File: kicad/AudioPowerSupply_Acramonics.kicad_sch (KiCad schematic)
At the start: 32 parts, among them J1 Conn_01x02_Pin, J6 GND 48V, J7 Conn_01x03_Pin, J8 Conn_01x03_Pin, T1 12-0-12V, U1 LM7815_TO220, U2 LM7915_TO220, U3 LM317_TO-220

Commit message: Put 48V circuit on separate diagram
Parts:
- removed C10, C11: 100nF, Capacitor_THT:C_Rect_L7.2mm_W3.0mm_P5.00mm_FKS2_FKP2_MKS2_MKP2, symbol Device:C_Small
- removed C3, C4: 100uF 100V, Capacitor_THT:CP_Radial_D12.5mm_P5.00mm, symbol Device:C_Polarized_Small
- removed C5: 220uF 100V, Capacitor_THT:CP_Radial_D12.5mm_P5.00mm, symbol Device:C_Polarized_Small
- removed D1: 1N4003, Diode_THT:D_DO-41_SOD81_P10.16mm_Horizontal, symbol Diode:1N4003
- removed D2, D3, D4, D5: 1N4004, Diode_THT:D_DO-41_SOD81_P10.16mm_Horizontal, symbol Diode:1N4004
- removed J6: GND 48V, Connector_Molex:Molex_KK-254_AE-6410-02A_1x02_P2.54mm_Vertical, symbol Connector:Conn_01x02_Pin
- removed R1: 8K2 2W, Resistor_THT:R_Axial_DIN0414_L11.9mm_D4.5mm_P15.24mm_Horizontal, symbol Device:R_Small
- removed R2: 240R, Resistor_THT:R_Axial_DIN0207_L6.3mm_D2.5mm_P10.16mm_Horizontal, symbol Device:R_Small
- removed U3: LM317_TO-220, Package_TO_SOT_THT:TO-220-3_Vertical, symbol Regulator_Linear:LM317_TO-220
- J1: footprint (none) -> TerminalBlock_Altech:Altech_AK100_1x02_P5.00mm
- J7, J8: footprint TerminalBlock_4Ucon:TerminalBlock_4Ucon_1x03_P3.50mm_Horizontal -> TerminalBlock_Altech:Altech_AK100_1x03_P5.00mm
- renumbered C6 to C3, C7 to C4, C12 to C5, C13 to C6, C8 to C7, C9 to C8, D6 to D1, D7 to D2, D8 to D3, D9 to D4
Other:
- added sheet 48V-Booster (48V-Booster.kicad_sch)

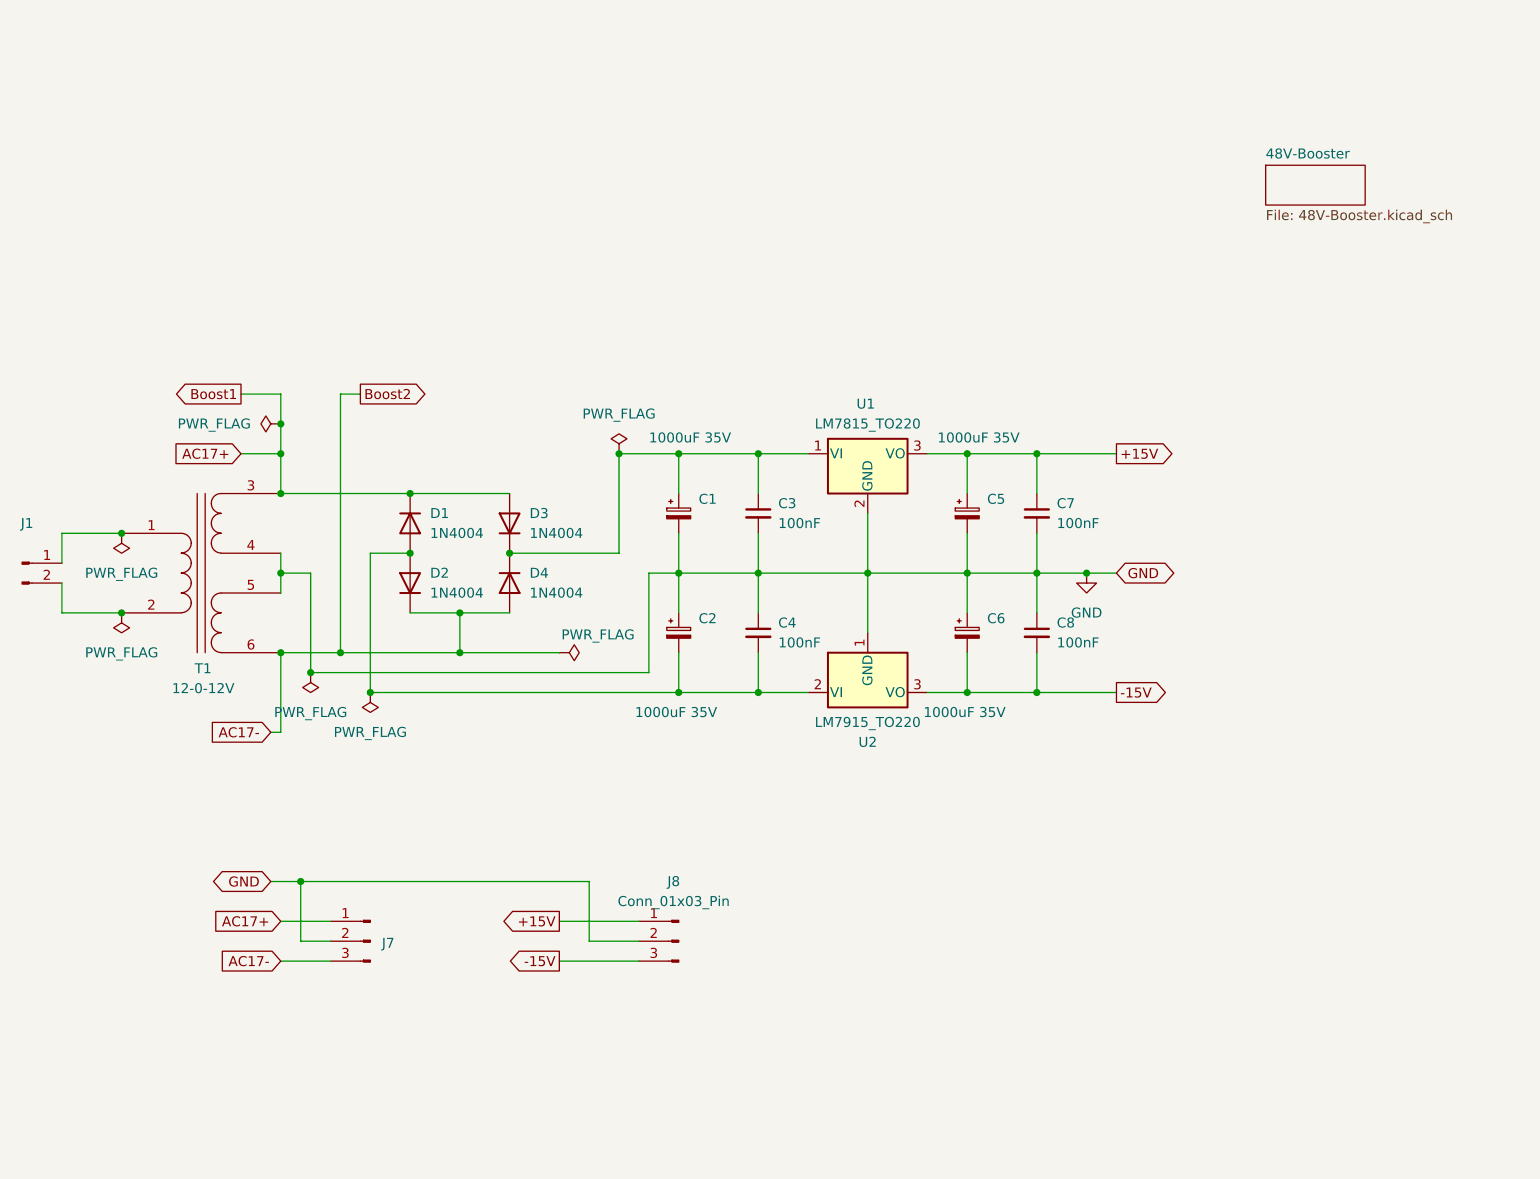
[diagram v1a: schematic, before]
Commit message: Board done - needs added text
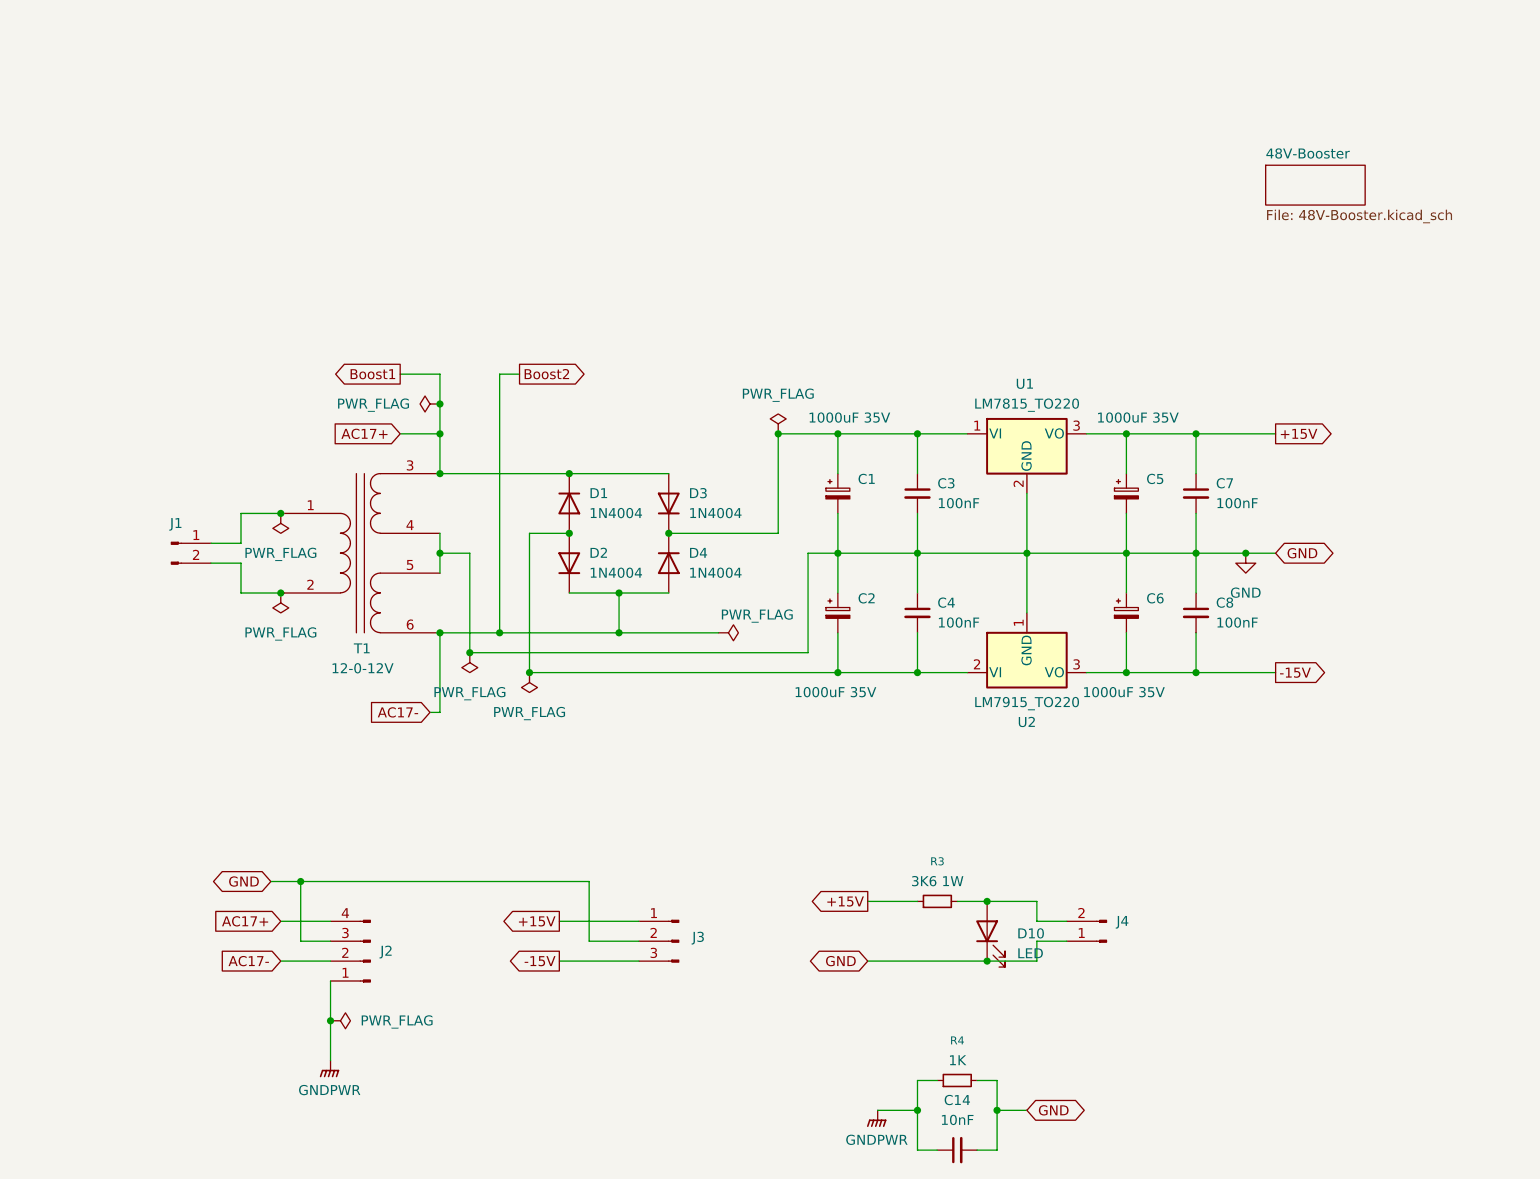
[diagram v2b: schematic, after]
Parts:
- removed J7: Conn_01x03_Pin, TerminalBlock_Altech:Altech_AK100_1x03_P5.00mm, symbol Connector:Conn_01x03_Pin
- added C14: 10nF, Capacitor_THT:C_Rect_L7.2mm_W3.0mm_P5.00mm_FKS2_FKP2_MKS2_MKP2, symbol Device:C_Small
- added D10: LED, symbol Device:LED
- added J2: Conn_01x04_Pin, TerminalBlock_Altech:Altech_AK100_1x04_P5.00mm, symbol Connector:Conn_01x04_Pin
- added J4: (no value), Connector_Molex:Molex_KK-254_AE-6410-02A_1x02_P2.54mm_Vertical, symbol Connector:Conn_01x02_Pin
- added R3: 3K6 1W, Resistor_THT:R_Axial_DIN0414_L11.9mm_D4.5mm_P15.24mm_Horizontal, symbol Device:R_Small
- added R4: 1K, Resistor_THT:R_Axial_DIN0207_L6.3mm_D2.5mm_P10.16mm_Horizontal, symbol Device:R_Small
- J1: value Conn_01x02_Pin -> (none); footprint TerminalBlock_Altech:Altech_AK100_1x02_P5.00mm -> (none)
- J3: renamed from J8; value Conn_01x03_Pin -> (none)
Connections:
- net +15V: now also R3.1
- net AC17+: now also J2.4 (Pin_4)
- net AC17-: now also J2.2 (Pin_2)
- net GND: now also C14.2, D10.1 (K), J2.3 (Pin_3), J4.1 (Pin_1), R4.2
- new net: D10.2 (A), J4.2 (Pin_2), R3.2
- new net GNDPWR: C14.1, J2.1 (Pin_1), R4.1
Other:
- moved on the sheet: C1, C2, C3, C4, C5, C6, C7, C8, D1, D2, D3, D4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
